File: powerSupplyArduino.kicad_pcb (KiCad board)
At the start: 2 copper layers, 90 x 50 mm, 61 parts, among them J1 supply_shunt, J2 Main connector, J3 Display, J4 Termo_sens, J5 ISP, J6 Encoder, U1 LM324, U2 TL494, U3 ATmega8A-AU

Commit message: changes for pcbway
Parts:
- added H1: , Mounting_Holes:MountingHole_3.2mm_M3_Pad_Via, F.Cu at (94.7, 95.4)
- added H2: , Mounting_Holes:MountingHole_3.2mm_M3_Pad_Via, F.Cu at (166.8, 95.4)
- added J10: GND, Pin_Headers:Pin_Header_Straight_1x01_Pitch2.54mm, F.Cu at (156.1, 59.0)
- added J11: +5v, Pin_Headers:Pin_Header_Straight_1x01_Pitch2.54mm, F.Cu at (132.9, 96.7)
- added J12: Fun ctrl, Pin_Headers:Pin_Header_Straight_1x01_Pitch2.54mm, F.Cu at (120.4, 96.5)
- added J7: +15v, Pin_Headers:Pin_Header_Straight_1x01_Pitch2.54mm, F.Cu at (151.5, 85.5)
- added J8: Supply, Pin_Headers:Pin_Header_Straight_1x02_Pitch2.54mm, F.Cu at (152.7, 53.0)
- C1, C16, R21, R23, R25, R27: moved to F.Cu
- J1: value supply_shunt -> Q3b; footprint Pin_Headers:Pin_Header_Straight_1x04_Pitch2.54mm -> Pin_Headers:Pin_Header_Straight_1x01_Pitch2.54mm
- J2: value Main connector -> Q4b; footprint Pin_Headers:Pin_Header_Angled_1x10_Pitch2.54mm -> Pin_Headers:Pin_Header_Straight_1x01_Pitch2.54mm
- moved R26 35.8 mm to (126.3, 90.3)
- moved R22 35.2 mm to (153.1, 70.8)
- moved C18 31.3 mm to (97.1, 84.4), turned to 180 degrees
- moved R7 31.2 mm to (122.0, 64.0), turned to 0 degrees
- moved C7 30.4 mm to (123.3, 58.7), turned to 90 degrees
- moved C10 29.9 mm to (96.7, 53.1)
- moved R24 28.6 mm to (147.3, 70.8), turned to 180 degrees
- moved J1 28.4 mm to (151.5, 80.7), turned to 0 degrees
- moved R21 23.4 mm to (141.5, 70.8), turned to 180 degrees
- moved J2 23.2 mm to (151.4, 75.8), turned to 0 degrees
- moved L1 18.1 mm to (127.6, 96.9), turned to 180 degrees
- moved R3 13.5 mm to (140.2, 52.9)
- moved C1 10.5 mm to (146.9, 53.0)
- moved R25 9.32 mm to (133.6, 90.3), turned to 180 degrees
- moved R23 7.45 mm to (153.4, 64.0), turned to 180 degrees
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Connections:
- J1 pad 1: GND -> Q3Base
- J2 pad 1: FAN_CNTR -> Q4Base
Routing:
- net GND: track 415.0 -> 0.00 mm
- net +5V: track 274.9 -> 0.00 mm, vias 2 -> 0
- net +15V: track 129.6 -> 0.00 mm, vias 3 -> 0
- net Supply-: track 120.7 -> 0.00 mm
- net Encoder_S: track 109.9 -> 0.00 mm, vias 1 -> 0
- net Q3Base: track 109.1 -> 0.00 mm
- net Net-(R12-Pad1): track 107.0 -> 0.00 mm
- net Net-(R10-Pad1): track 85.8 -> 0.00 mm, vias 1 -> 0
- net Encoder_A: track 85.2 -> 0.00 mm, vias 1 -> 0
- net Net-(C20-Pad1): track 81.6 -> 0.00 mm, vias 1 -> 0
- net ISP_VCC: track 77.3 -> 0.00 mm, vias 1 -> 0
- net Net-(C7-Pad2): track 71.5 -> 0.00 mm, vias 2 -> 0
- net Q4Base: track 71.1 -> 0.00 mm, vias 1 -> 0
- net Encoder_B: track 71.1 -> 0.00 mm, vias 1 -> 0
- net Net-(R8-Pad1): track 69.2 -> 0.00 mm, vias 1 -> 0
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- removed copper zone on B.Cu, net GND
- removed copper zone on F.Cu, net GND
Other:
- outline, holes or cut-outs redrawn
- net class +15 added: clearance 0.2, trace_width 0.8, via_dia 1, via_drill 0.7
- net class +5 added: clearance 0.2, trace_width 0.9, via_dia 1, via_drill 0.7
- net class Default: via_dia 1.3 -> 1
- net class gnd added: clearance 0.2, trace_width 1, via_dia 1, via_drill 0.7

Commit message: new positions
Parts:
- moved J4 2.32 mm to (92.1, 87.3), turned to 180 degrees
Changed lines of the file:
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@@
     (add_net FAN_CNTR)
     (add_net ISP_RESET)
-    (add_net ISP_VCC)
     (add_net LED_CUR)
     (add_net MISO)
@@
     (add_net "Net-(R8-Pad1)")
     (add_net "Net-(R9-Pad1)")
-    (add_net "Net-(U3-Pad1)")
-    (add_net "Net-(U3-Pad19)")
-    (add_net "Net-(U3-Pad22)")
-    (add_net "Net-(U3-Pad27)")
-    (add_net "Net-(U3-Pad28)")
     (add_net Q3Base)
     (add_net Q4Base)
@@
     (uvia_dia 0.3)
     (uvia_drill 0.1)
+    (add_net ISP_VCC)
     (add_net Supply+)
     (add_net Supply-)
@@
   )
   (module Pin_Headers:Pin_Header_Straight_1x02_Pitch2.54mm (layer F.Cu)
-    (at 91.95 84.97)
+    (at 92.08 87.29 180)
     (descr "Through hole straight pin header, 1x02, 2.54mm pitch, single row")
     (tags "Through hole pin header THT 1x02 2.54mm single row")
@@
     (fp_line (start 1.8 4.35) (end 1.8 -1.8) (layer F.CrtYd) (width 0.05))
     (fp_line (start 1.8 -1.8) (end -1.8 -1.8) (layer F.CrtYd) (width 0.05))
-    (fp_text user %R (at 0 1.27 -270) (layer F.Fab)
-      (effects (font (size 1 1) (thickness 0.15)))
-    )
-    (pad 1 thru_hole rect (at 0 0) (size 1.7 1.7) (drill 1) (layers *.Cu *.Mask)
+    (fp_text user %R (at 0 1.27 90) (layer F.Fab)
+      (effects (font (size 1 1) (thickness 0.15)))
+    )
+    (pad 1 thru_hole rect (at 0 0 180) (size 1.7 1.7) (drill 1) (layers *.Cu *.Mask)
       (net 34 TERMO_SENS))
-    (pad 2 thru_hole oval (at 0 2.54) (size 1.7 1.7) (drill 1) (layers *.Cu *.Mask)
+    (pad 2 thru_hole oval (at 0 2.54 180) (size 1.7 1.7) (drill 1) (layers *.Cu *.Mask)
       (net 2 GND))
     (model ${KISYS3DMOD}/Pin_Headers.3dshapes/Pin_Header_Straight_1x02_Pitch2.54mm.wrl
@@
   (gr_line (start 90 50) (end 180 50) (layer Edge.Cuts) (width 0.05))
   (gr_line (start 180 50) (end 180 100) (layer Edge.Cuts) (width 0.05))
+  (zone (net 0) (net_name "") (layer F.Cu) (hatch edge 0.508)
+    (connect_pads (clearance 0))
+    (min_thickness 0.254)
+    (keepout (tracks not_allowed) (vias not_allowed) (copperpour allowed))
+    (fill (arc_segments 32) (thermal_gap 0.508) (thermal_bridge_width 0.508))
+    (polygon
+      (pts
+        (xy 116.24 77.8) (xy 114.95 75.62) (xy 119.94 75.54) (xy 118.61 77.8)
+      )
+    )
+  )
 )

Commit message: gerber
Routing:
- net GND: track 0.00 -> 454.5 mm, vias 0 -> 3
- net +5V: track 0.00 -> 159.6 mm, vias 0 -> 4
- net Net-(C20-Pad1): track 0.00 -> 98.7 mm
- net Net-(C12-Pad1): track 0.00 -> 95.9 mm
- net Encoder_S: track 0.00 -> 95.6 mm, vias 0 -> 1
- net Supply-: track 0.00 -> 89.5 mm, vias 0 -> 1
- net Net-(R10-Pad1): track 0.00 -> 87.5 mm
- net +15V: track 0.00 -> 84.0 mm, vias 0 -> 1
- net ISP_VCC: track 0.00 -> 75.0 mm, vias 0 -> 1
- net Net-(C9-Pad1): track 0.00 -> 68.7 mm
- net Encoder_A: track 0.00 -> 63.8 mm, vias 0 -> 1
- net Net-(R12-Pad1): track 0.00 -> 60.8 mm, vias 0 -> 2
- net Net-(R8-Pad1): track 0.00 -> 58.7 mm, vias 0 -> 1
- net Net-(R14-Pad2): track 0.00 -> 58.4 mm, vias 0 -> 2
- net Net-(R26-Pad1): track 0.00 -> 57.4 mm
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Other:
- board text added: "poverSupplyArduino 0.1"

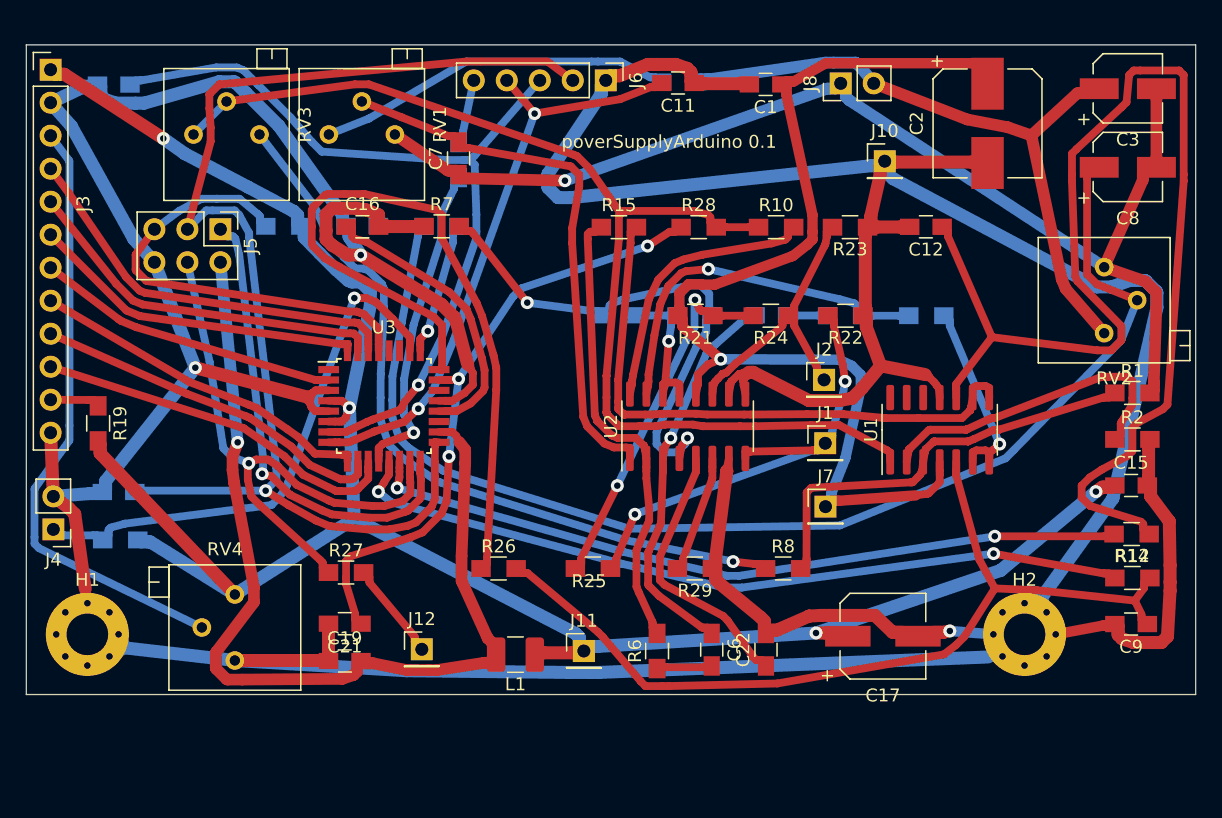
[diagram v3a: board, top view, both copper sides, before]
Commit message: v .2 fixed intersect of mount pad and some track
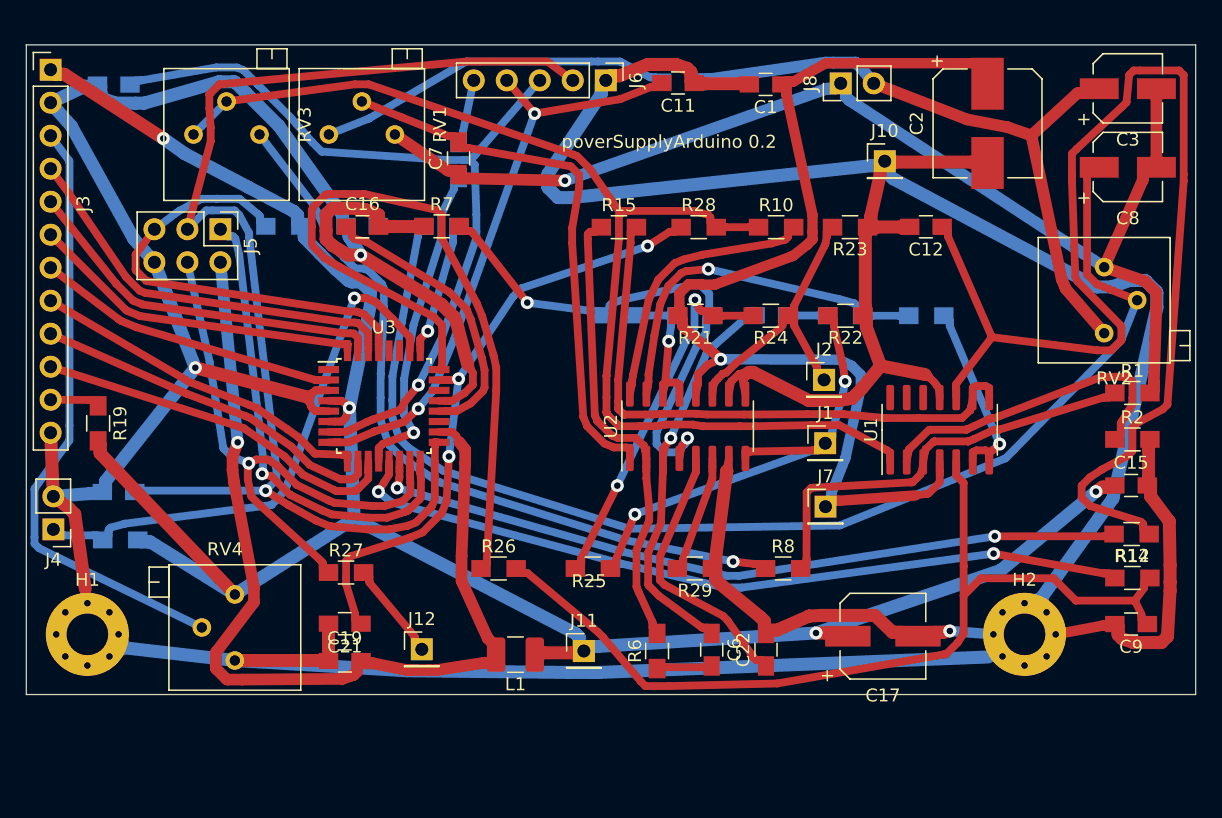
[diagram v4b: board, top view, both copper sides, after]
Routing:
- net Net-(C9-Pad1): track 68.7 -> 71.3 mm
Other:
- board text added: "poverSupplyArduino 0.2"
- board text removed: "poverSupplyArduino 0.1"
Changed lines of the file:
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@@
     )
   )
-  (gr_text "poverSupplyArduino 0.1" (at 139.47 57.46) (layer F.SilkS)
+  (gr_text "poverSupplyArduino 0.2" (at 139.47 57.46) (layer F.SilkS)
     (effects (font (size 1 1) (thickness 0.15)))
   )
@@
   (segment (start 174.271 72.746) (end 174.2801 72.7239) (width 0.6) (layer B.Cu) (net 11))
   (segment (start 174.2801 72.7239) (end 175.5 69.65) (width 0.6) (layer B.Cu) (net 11))
-  (segment (start 164.5441 91.832) (end 167.7776 91.9699) (width 0.6) (layer F.Cu) (net 12))
-  (segment (start 167.7776 91.9699) (end 175.3193 92.7719) (width 0.6) (layer F.Cu) (net 12))
   (segment (start 176.28 94.575) (end 175.83 94.25) (width 0.6) (layer F.Cu) (net 12))
   (segment (start 175.83 94.25) (end 175.83 93.95) (width 0.6) (layer F.Cu) (net 12))
   (segment (start 175.83 93.95) (end 175.83 93.8257) (width 0.6) (layer F.Cu) (net 12))
   (segment (start 175.83 93.8257) (end 175.3193 92.7719) (width 0.6) (layer F.Cu) (net 12))
-  (segment (start 127.7 90.3) (end 128.15 90.65) (width 0.6) (layer F.Cu) (net 12))
-  (segment (start 128.15 90.65) (end 128.45 90.65) (width 0.6) (layer F.Cu) (net 12))
-  (segment (start 128.45 90.65) (end 128.5743 90.65) (width 0.6) (layer F.Cu) (net 12))
-  (segment (start 128.5743 90.65) (end 134.0086 95.1999) (width 0.6) (layer F.Cu) (net 12))
-  (segment (start 134.0086 95.1999) (end 134.3601 95.5514) (width 0.6) (layer F.Cu) (net 12))
-  (segment (start 134.3601 95.5514) (end 137.2979 98.9986) (width 0.6) (layer F.Cu) (net 12))
-  (segment (start 137.2979 98.9986) (end 137.6494 99.3501) (width 0.6) (layer F.Cu) (net 12))
-  (segment (start 137.6494 99.3501) (end 138.9494 99.3501) (width 0.6) (layer F.Cu) (net 12))
-  (segment (start 138.9494 99.3501) (end 139.4466 99.3501) (width 0.6) (layer F.Cu) (net 12))
-  (segment (start 139.4466 99.3501) (end 147.8036 99.1501) (width 0.6) (layer F.Cu) (net 12))
-  (segment (start 147.8036 99.1501) (end 160.6286 96.9101) (width 0.6) (layer F.Cu) (net 12))
-  (segment (start 160.6286 96.9101) (end 161.5358 96.2087) (width 0.6) (layer F.Cu) (net 12))
-  (segment (start 161.5358 96.2087) (end 162.1802 95.5643) (width 0.6) (layer F.Cu) (net 12))
-  (segment (start 162.1802 95.5643) (end 164.5441 91.832) (width 0.6) (layer F.Cu) (net 12))
-  (segment (start 164.5441 91.832) (end 163.3463 89.6089) (width 0.6) (layer F.Cu) (net 12))
-  (segment (start 163.3463 89.6089) (end 161.57 83.1412) (width 0.6) (layer F.Cu) (net 12))
-  (segment (start 161.57 83.1412) (end 161.57 83.0706) (width 0.6) (layer F.Cu) (net 12))
-  (segment (start 161.57 83.0706) (end 161.57 82.7706) (width 0.6) (layer F.Cu) (net 12))
-  (segment (start 161.57 82.7706) (end 161.57 82.095) (width 0.6) (layer F.Cu) (net 12))
   (segment (start 176.48 91.03) (end 176.03 91.38) (width 0.6) (layer F.Cu) (net 12))
   (segment (start 176.03 91.38) (end 176.03 91.68) (width 0.6) (layer F.Cu) (net 12))
   (segment (start 176.03 91.68) (end 176.03 91.8043) (width 0.6) (layer F.Cu) (net 12))
   (segment (start 176.03 91.8043) (end 175.3193 92.7719) (width 0.6) (layer F.Cu) (net 12))
+  (segment (start 139.4466 99.3501) (end 137.6494 99.3501) (width 0.6) (layer F.Cu) (net 12))
+  (segment (start 137.6494 99.3501) (end 137.2979 98.9986) (width 0.6) (layer F.Cu) (net 12))
+  (segment (start 161.57 82.095) (end 161.57 83.1412) (width 0.6) (layer F.Cu) (net 12))
+  (segment (start 128.5743 90.65) (end 128.15 90.65) (width 0.6) (layer F.Cu) (net 12))
+  (segment (start 134.0086 95.1999) (end 128.5743 90.65) (width 0.6) (layer F.Cu) (net 12))
+  (segment (start 147.8036 99.1501) (end 139.4466 99.3501) (width 0.6) (layer F.Cu) (net 12))
+  (segment (start 160.6286 96.9101) (end 147.8036 99.1501) (width 0.6) (layer F.Cu) (net 12))
+  (segment (start 137.2979 98.9986) (end 134.3601 95.5514) (width 0.6) (layer F.Cu) (net 12))
+  (segment (start 128.15 90.65) (end 127.7 90.3) (width 0.6) (layer F.Cu) (net 12))
+  (segment (start 134.3601 95.5514) (end 134.0086 95.1999) (width 0.6) (layer F.Cu) (net 12))
+  (segment (start 162.143055 83.714255) (end 161.57 83.1412) (width 0.6) (layer F.Cu) (net 12))
+  (segment (start 160.781845 96.9101) (end 161.687288 96.004657) (width 0.6) (layer F.Cu) (net 12))
+  (segment (start 161.687288 96.004657) (end 162.143055 95.31286) (width 0.6) (layer F.Cu) (net 12))
+  (segment (start 160.6286 96.9101) (end 160.781845 96.9101) (width 0.6) (layer F.Cu) (net 12))
+  (segment (start 163.47 91.05) (end 162.143055 92.376945) (width 0.6) (layer F.Cu) (net 12))
+  (segment (start 169.06 91.05) (end 163.47 91.05) (width 0.6) (layer F.Cu) (net 12))
+  (segment (start 175.3193 92.7719) (end 170.7819 92.7719) (width 0.6) (layer F.Cu) (net 12))
+  (segment (start 162.143055 95.31286) (end 162.143055 92.376945) (width 0.6) (layer F.Cu) (net 12))
+  (segment (start 170.7819 92.7719) (end 169.06 91.05) (width 0.6) (layer F.Cu) (net 12))
+  (segment (start 162.143055 92.376945) (end 162.143055 90.113055) (width 0.6) (layer F.Cu) (net 12))
+  (segment (start 162.143055 90.113055) (end 162.143055 83.714255) (width 0.6) (layer F.Cu) (net 12))
   (segment (start 113.27 79.79) (end 113.77 79.79) (width 0.6) (layer F.Cu) (net 13))
   (segment (start 113.77 79.79) (end 114.07 79.79) (width 0.6) (layer F.Cu) (net 13))
